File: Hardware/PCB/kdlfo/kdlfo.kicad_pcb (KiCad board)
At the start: 2 copper layers, 71 x 168 mm, 83 parts, among them J1 3_pin_Molex_header, J10 AudioJack2, J11 AudioJack2, J12 AudioJack2, J13 AudioJack2, J14 AudioJack2, J15 Synth_power_2x5, J2 3_pin_Molex_header, J3 3_pin_Molex_header, J7 3_pin_Molex_header, J9 AudioJack2, Q1 2N3904, Q2 2N3904, Q3 2N3904, Q4 2N3904, U1 TL074, U2 TL072, U3 TL074, U4 TL072

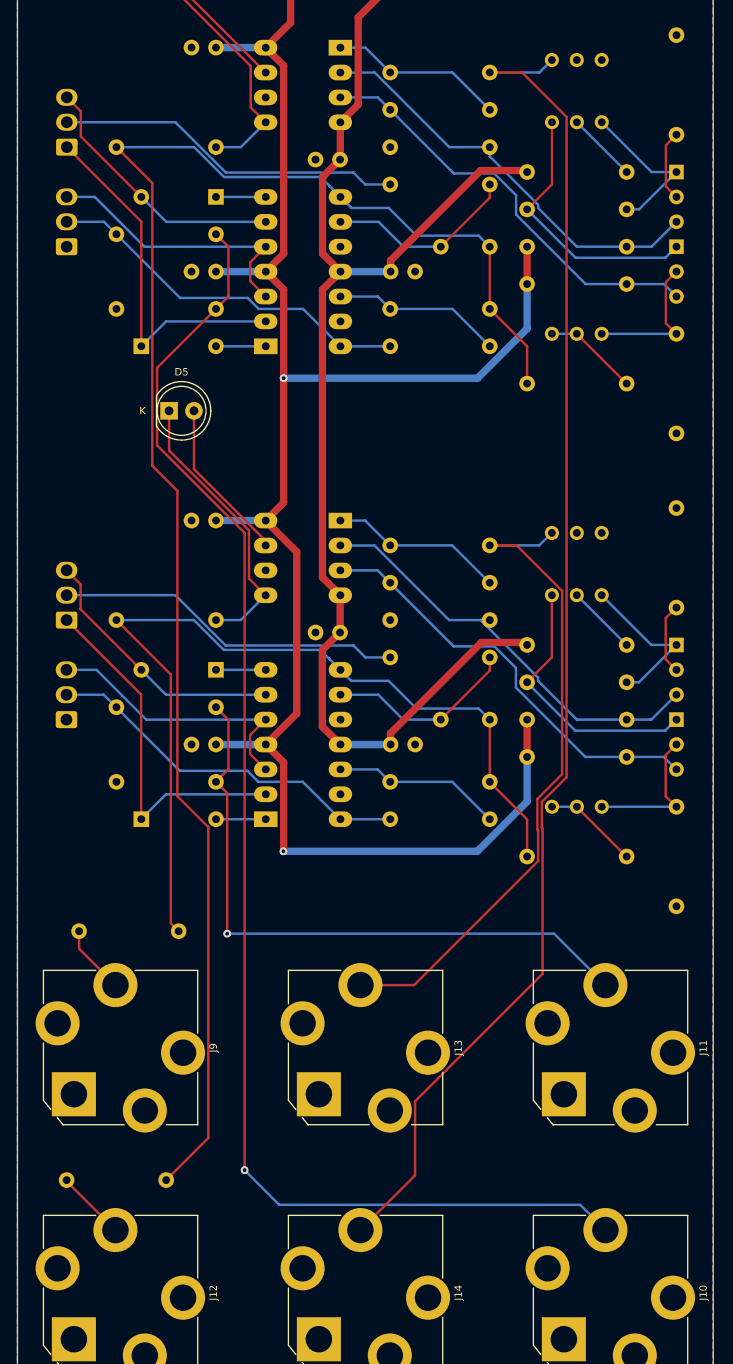
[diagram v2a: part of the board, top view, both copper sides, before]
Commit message: Reorg schematic, redo layout some more
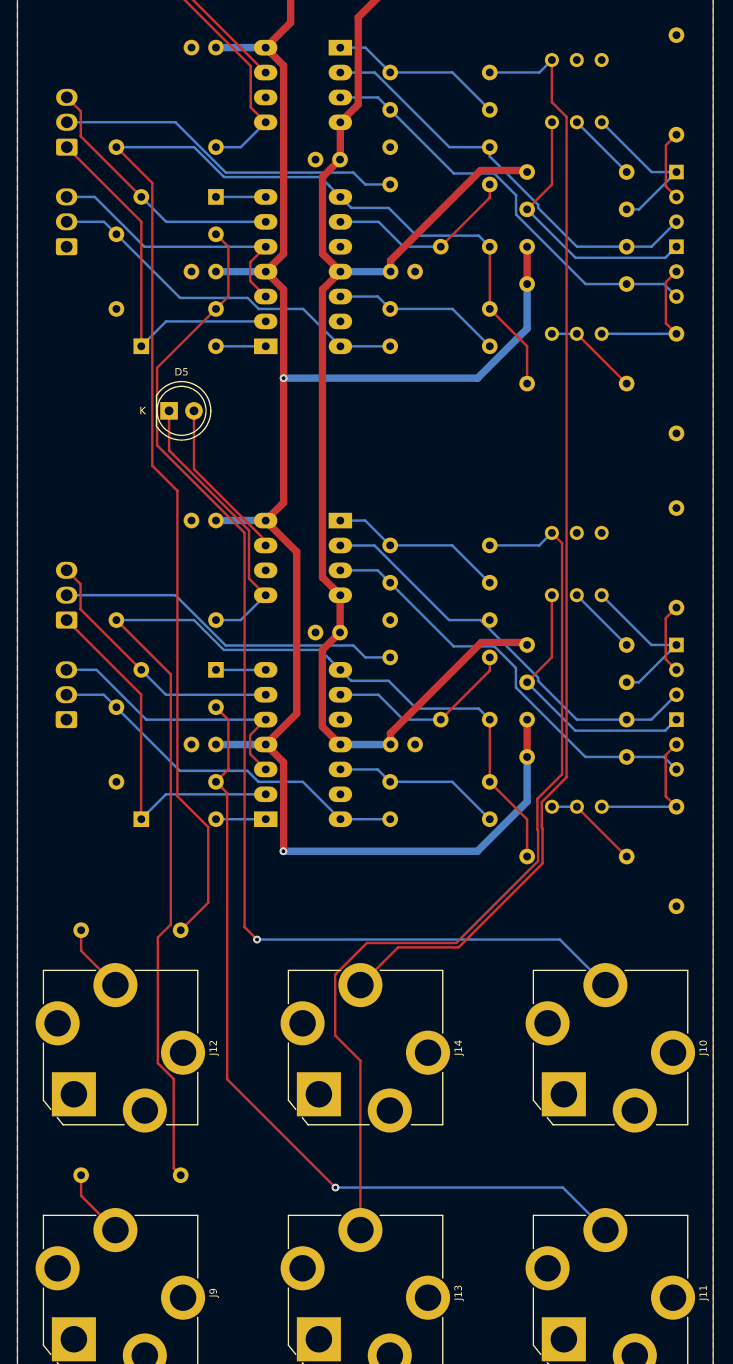
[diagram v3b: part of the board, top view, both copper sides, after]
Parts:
- moved R12 25.5 mm to (71.0, 153.0)
- moved J10 25.0 mm to (125.0, 165.0)
- moved J11 25.0 mm to (125.0, 190.0)
- moved J12 25.0 mm to (75.0, 165.0)
- moved J13 25.0 mm to (100.0, 190.0)
- moved J14 25.0 mm to (100.0, 165.0)
- moved J9 25.0 mm to (75.0, 190.0)
- moved R31 24.9 mm to (71.0, 178.0)
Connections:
- net /LFO A/SINE renamed /SINE_A
- net /LFO A/SQPULSE renamed /SQPULSE_A
- net /LFO A/TRIRAMP renamed /TRIRAMP_A
- net /LFO B/SINE renamed /SINE_B
- net /LFO B/SQPULSE renamed /SQPULSE_B
- net /LFO B/TRIRAMP renamed /TRIRAMP_B
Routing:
- net /SINE_B: track 68.2 -> 94.5 mm
- net Net-(C2-Pad1): track 168.9 -> 142.8 mm
- net Net-(C1-Pad1): track 92.3 -> 118.3 mm
- net /SQPULSE_A: track 142.1 -> 117.2 mm
- net /SINE_A: track 139.0 -> 114.3 mm
- net /SQPULSE_B: track 65.4 -> 84.5 mm

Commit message: Fix LED
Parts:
- C1, C2: value 220n -> 220n/2.2uF
- R14, R28: value 4.7k -> RL
- moved D7 12.0 mm to (92.4, 51.5), turned to 90 degrees
- moved C3 5.08 mm to (87.3, 51.5)
- moved C7 5.08 mm to (115.2, 51.5)
- moved D8 3.81 mm to (107.6, 41.3), turned to -90 degrees
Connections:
- R14 pad 2: Net-(C2-Pad1) -> GND
- R28 pad 2: Net-(C1-Pad1) -> GND
- U2 pad 5: Net-(D6-Pad1) -> Net-(C2-Pad1)
- U2 pad 6: GND -> Net-(D6-Pad1)
- U4 pad 5: Net-(D5-Pad1) -> Net-(C1-Pad1)
- U4 pad 6: GND -> Net-(D5-Pad1)
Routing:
- net Net-(C1-Pad1): track 118.3 -> 106.7 mm
- net Net-(C2-Pad1): track 142.8 -> 132.3 mm
- net +12V: track 230.9 -> 223.2 mm
- net Net-(D5-Pad2): track 16.3 -> 21.8 mm
- net /LFO A/SHPOTW: track 35.6 -> 38.7 mm
- net /LFO B/SHPOTW: track 35.7 -> 38.7 mm
- net /SQPULSE_A: track 117.2 -> 120.1 mm
- net /-12_IN: track 14.3 -> 16.6 mm
- net Net-(D6-Pad1): track 43.3 -> 41.8 mm
- net Net-(D5-Pad1): track 29.0 -> 30.3 mm
- net /+12_IN: track 9.94 -> 9.42 mm

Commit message: Final pre fab tweaks, Gerbers
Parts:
- added GRAF2: CC0 logo, ao_tht:CC0_logo, B.Cu at (81.5, 106.0)
- added GRAF3: AO logo, ao_tht:analogoutput_12mm, B.Cu at (100.0, 149.5)
- C1: value 220n/2.2uF -> 220n
- C2: value 220n/2.2uF -> 2.2uF; footprint ao_tht:C_Rect_L7.2mm_W7.2mm_P5.00mm_FKS2_FKP2_MKS2_MKP2 -> ao_tht:C_Radial_D5.0mm_H11.0mm_P2.00mm
- D3: renamed from D2; footprint Diode_THT:D_DO-35_SOD27_P7.62mm_Horizontal -> ao_tht:D_DO-35_SOD27_P7.62mm_Horizontal
- D4: footprint Diode_THT:D_DO-35_SOD27_P7.62mm_Horizontal -> ao_tht:D_DO-35_SOD27_P7.62mm_Horizontal
- D6: renamed from D1; footprint Diode_THT:D_DO-35_SOD27_P7.62mm_Horizontal -> ao_tht:D_DO-35_SOD27_P7.62mm_Horizontal
- D7: renamed from D3; footprint Diode_THT:D_DO-35_SOD27_P7.62mm_Horizontal -> ao_tht:D_DO-35_SOD27_P7.62mm_Horizontal
- R19: renamed from R3; value 100 -> 100R
- R2: value 100 -> 100R
- RV10: renamed from RV9; value B5K -> B5k
- RV5: renamed from RV6; value B50K -> B50k
- RV7: renamed from RV8; value B5K -> B5k
- RV8: renamed from RV5; value B50K -> B50k
- moved C1 48.5 mm to (107.6, 83.2), turned to 0 degrees
- moved C2 48.5 mm to (107.6, 131.5), turned to 0 degrees
- renumbered C12 to C10, C9 to C11, C10 to C12, C7 to C4, C4 to C5, C8 to C6, C5 to C7, C6 to C8, C11 to C9, D7 to D1, D8 to D2, D6 to D5, D5 to D8, J3 to J1, J7 to J2, J1 to J3, J2 to J4, J12 to J5, J14 to J6, J11 to J7, J9 to J8, J13 to J9, Q3 to Q1, Q4 to Q2, Q1 to Q3, Q2 to Q4, R22 to R1, R4 to R10, R25 to R11, R6 to R12, R20 to R13, R10 to R14, R12 to R15, R26 to R16, R14 to R17, R1 to R18, R5 to R20, R7 to R21, R8 to R22, R11 to R23, R13 to R24, R15 to R25, R16 to R26, R17 to R27, R21 to R28, R23 to R29, R29 to R3, R24 to R30, R27 to R31, R31 to R32, R28 to R34, R18 to R4, R32 to R5, R9 to R6, R19 to R7, R34 to R8, R30 to R9, RV10 to RV6, RV7 to RV9
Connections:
- C1 pad 1: Net-(C1-Pad1) -> /LFO A/CAP1
- C1 pad 2: Net-(C1-Pad2) -> /LFO A/CAP2
- C2 pad 1: Net-(C2-Pad1) -> /LFO B/CAP1
- C2 pad 2: Net-(C2-Pad2) -> /LFO B/CAP2
- J1 pad 1: /LFO A/SHPOTCW -> /LFO A/SHPOTCCW
- J1 pad 3: /LFO A/SHPOTCCW -> /LFO A/SHPOTCW
- J2 pad 2: /LFO A/FRPOTCW -> /LFO A/FRPOTW
- J2 pad 3: /LFO A/FRPOTW -> /LFO A/FRPOTCW
- J3 pad 1: /LFO B/SHPOTCW -> /LFO B/SHPOTCCW
- J3 pad 3: /LFO B/SHPOTCCW -> /LFO B/SHPOTCW
- J4 pad 2: /LFO B/FRPOTCW -> /LFO B/FRPOTW
- J4 pad 3: /LFO B/FRPOTW -> /LFO B/FRPOTCW
- Q1 pad 2: Net-(Q3-Pad2) -> Net-(Q1-Pad2)
- Q1 pad 3: Net-(Q3-Pad3) -> Net-(Q1-Pad3)
- Q2 pad 3: Net-(Q4-Pad3) -> Net-(Q2-Pad3)
- Q3 pad 2: Net-(Q1-Pad2) -> Net-(Q3-Pad2)
- Q3 pad 3: Net-(Q1-Pad3) -> Net-(Q3-Pad3)
- Q4 pad 3: Net-(Q2-Pad3) -> Net-(Q4-Pad3)
- R1 pad 2: Net-(C2-Pad1) -> /LFO A/CAP2
- R11 pad 1: Net-(Q4-Pad3) -> Net-(Q2-Pad3)
- R13 pad 2: Net-(Q3-Pad3) -> Net-(Q1-Pad3)
- R15 pad 2: Net-(C2-Pad1) -> /LFO A/CAP2
- R18 pad 2: Net-(C1-Pad1) -> /LFO B/CAP2
- R19 pad 2: Net-(C1-Pad2) -> /LFO B/CAP1
- R2 pad 2: Net-(C2-Pad2) -> /LFO A/CAP1
- R20 pad 1: Net-(Q1-Pad2) -> Net-(Q3-Pad2)
- R21 pad 2: Net-(Q1-Pad3) -> Net-(Q3-Pad3)
- R23 pad 2: Net-(C1-Pad1) -> /LFO B/CAP2
- R24 pad 2: Net-(Q2-Pad3) -> Net-(Q4-Pad3)
- R28 pad 1: Net-(Q2-Pad3) -> Net-(Q4-Pad3)
- R3 pad 1: Net-(Q3-Pad2) -> Net-(Q1-Pad2)
- R30 pad 2: Net-(Q1-Pad3) -> Net-(Q3-Pad3)
- R32 pad 2: Net-(C1-Pad1) -> /LFO B/CAP2
- R4 pad 2: Net-(Q3-Pad3) -> Net-(Q1-Pad3)
- R6 pad 2: Net-(C2-Pad1) -> /LFO A/CAP2
- R7 pad 2: Net-(Q4-Pad3) -> Net-(Q2-Pad3)
- RV10 pad 1: /SINE_B -> GND
- RV10 pad 2: GND -> /SINE_B
- RV10 pad 3: GND -> /SINE_B
- RV5 pad 1: /LFO A/SINE_ROUND -> Net-(Q1-Pad2)
- RV5 pad 3: Net-(Q3-Pad2) -> /LFO A/SINE_ROUND
- RV7 pad 1: /SINE_A -> GND
- RV7 pad 2: GND -> /SINE_A
- RV7 pad 3: GND -> /SINE_A
- RV8 pad 1: /LFO B/SINE_ROUND -> Net-(Q3-Pad2)
- RV8 pad 3: Net-(Q1-Pad2) -> /LFO B/SINE_ROUND
- U1 pad 8: Net-(C2-Pad1) -> /LFO A/CAP2
- U1 pad 9: Net-(C2-Pad2) -> /LFO A/CAP1
- U2 pad 2: Net-(Q4-Pad3) -> Net-(Q1-Pad3)
- U2 pad 3: Net-(Q3-Pad3) -> Net-(Q2-Pad3)
- U2 pad 5: Net-(C2-Pad1) -> /LFO A/CAP2
- U3 pad 8: Net-(C1-Pad1) -> /LFO B/CAP2
- U3 pad 9: Net-(C1-Pad2) -> /LFO B/CAP1
- U4 pad 2: Net-(Q2-Pad3) -> Net-(Q3-Pad3)
- U4 pad 3: Net-(Q1-Pad3) -> Net-(Q4-Pad3)
- U4 pad 5: Net-(C1-Pad1) -> /LFO B/CAP2
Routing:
- net Net-(C2-Pad1): track 132.3 -> 0.00 mm
- net /LFO A/CAP2: track 0.00 -> 131.5 mm
- net Net-(C1-Pad1): track 106.7 -> 0.00 mm
- net /LFO B/CAP2: track 0.00 -> 104.1 mm
- net Net-(C1-Pad2): track 19.7 -> 0.00 mm
- net /LFO B/CAP1: track 0.00 -> 19.7 mm
- net Net-(C2-Pad2): track 19.7 -> 0.00 mm
- net /LFO A/CAP1: track 0.00 -> 19.7 mm
- net /LFO B/SHPOTCW: track 37.2 -> 44.1 mm
- net /LFO A/SHPOTCW: track 37.2 -> 44.0 mm
- net /SINE_B: track 94.5 -> 100.7 mm
- net /SINE_A: track 114.3 -> 120.4 mm
- net Net-(Q1-Pad2): track 14.9 -> 20.8 mm
- net Net-(Q3-Pad2): track 14.9 -> 20.8 mm
- net /LFO B/SHPOTCCW: track 27.1 -> 23.5 mm
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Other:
- board text added: "Dual LFO"
- board text added: "FR CCW/W/CW"
- board text added: "Rich Holmes / April 2022 / CC0 1.0 Based on Kassutronics LFO http://github.com/holmesrichards/duallfo"
- board text added: "SH CCW/W/CW"

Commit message: Slotted jack footprints you idiot
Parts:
- J10, J5, J6, J7, J8, J9: footprint ao_tht:Jack_6.35mm_PJ_629HAN -> ao_tht:Jack_6.35mm_PJ_629HAN_slots

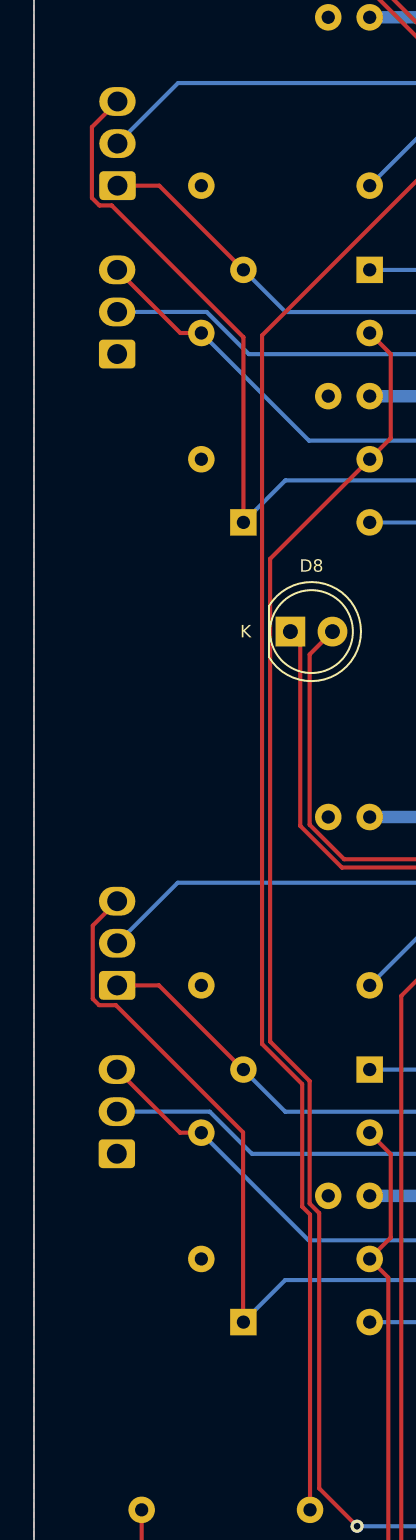
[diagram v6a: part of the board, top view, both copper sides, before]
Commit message: Fix silkscreen errors and omissions, change integ resistor, add shape resistor
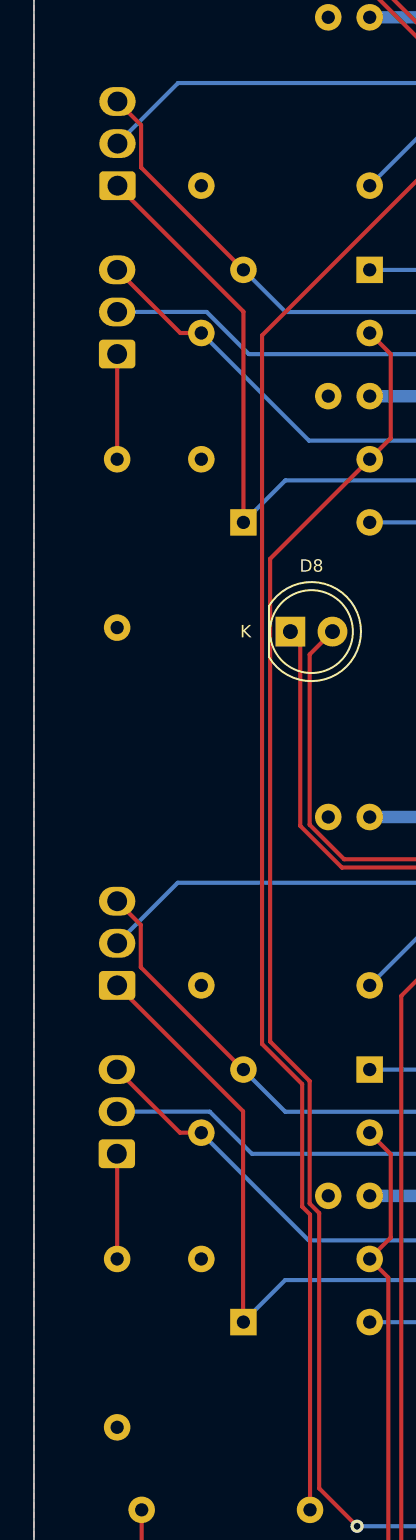
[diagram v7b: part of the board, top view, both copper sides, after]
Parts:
- added R35: 200R, ao_tht:R_Axial_DIN0207_L6.3mm_D2.5mm_P10.16mm_Horizontal, B.Cu at (69.5, 89.6)
- added R36: 200R, ao_tht:R_Axial_DIN0207_L6.3mm_D2.5mm_P10.16mm_Horizontal, B.Cu at (69.5, 137.9)
- R19, R2: value 100R -> 300R
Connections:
- D3 pad 1: /LFO A/SHPOTCW -> /LFO A/SHPOTCCW
- D4 pad 2: /LFO A/SHPOTCCW -> /LFO A/SHPOTCW
- D6 pad 1: /LFO B/SHPOTCW -> /LFO B/SHPOTCCW
- D7 pad 2: /LFO B/SHPOTCCW -> /LFO B/SHPOTCW
- J2 pad 1: GND -> /LFO A/FRPOTCCW
- J4 pad 1: GND -> /LFO B/FRPOTCCW
- U1 pad 2: /LFO A/SHPOTCW -> /LFO A/SHPOTCCW
- U1 pad 6: /LFO A/SHPOTCCW -> /LFO A/SHPOTCW
- U3 pad 2: /LFO B/SHPOTCW -> /LFO B/SHPOTCCW
- U3 pad 6: /LFO B/SHPOTCCW -> /LFO B/SHPOTCW
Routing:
- net /LFO B/SHPOTCW: track 44.1 -> 27.1 mm
- net /LFO A/SHPOTCW: track 44.0 -> 27.1 mm
- net /LFO B/SHPOTCCW: track 23.5 -> 37.2 mm
- net /LFO A/SHPOTCCW: track 23.5 -> 37.2 mm
- net /LFO B/FRPOTCCW: track 0.00 -> 6.36 mm
- net /LFO A/FRPOTCCW: track 0.00 -> 6.35 mm
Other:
- board text added: "FR CW/W/CCW"
- board text added: "SH CW/W/CCW"
- board text added: "Sine amplitude"
- board text added: "Sine roundness"
- board text added: "Sine symmetry"
- board text added: "Version 1.0"
- board text removed: "FR CCW/W/CW"
- board text removed: "SH CCW/W/CW"
